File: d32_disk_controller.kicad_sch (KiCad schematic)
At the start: 25 parts, among them J1 Clock_Test, J2 IDC_Floppy, J3 EDGE, U1 27C64, U2 WD2797, U3 74HCT174, U4 74HCT139, U5 74HCT00, U6 74HCT04, U7 74LS07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

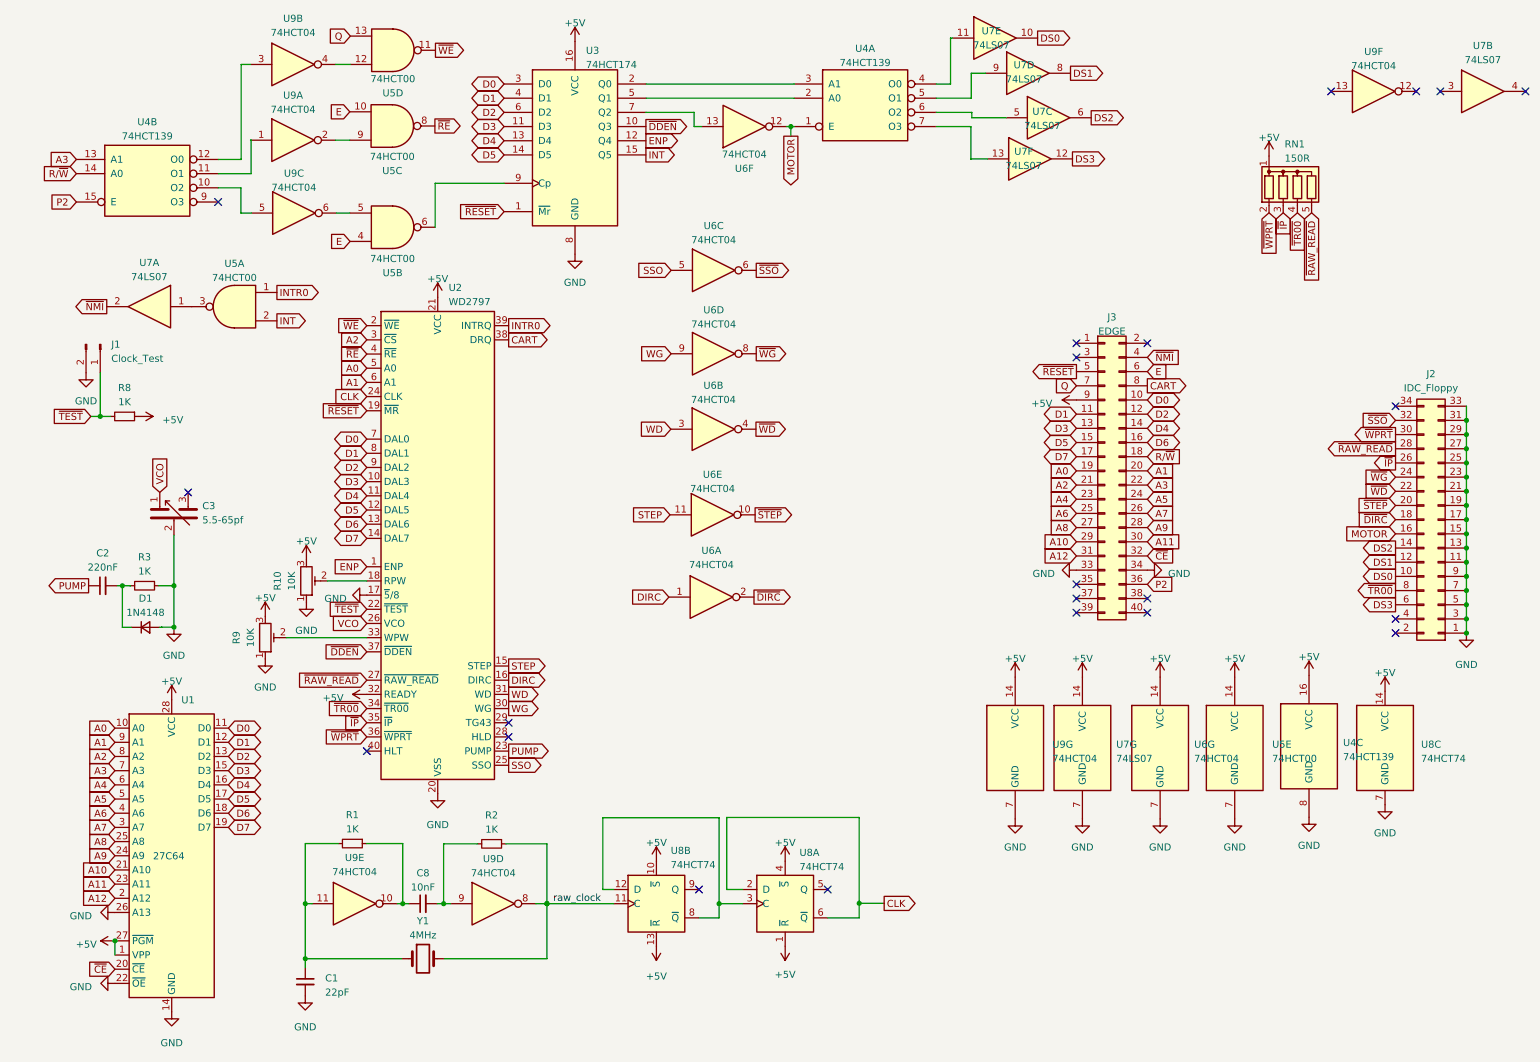
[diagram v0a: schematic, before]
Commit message: update from component selection change
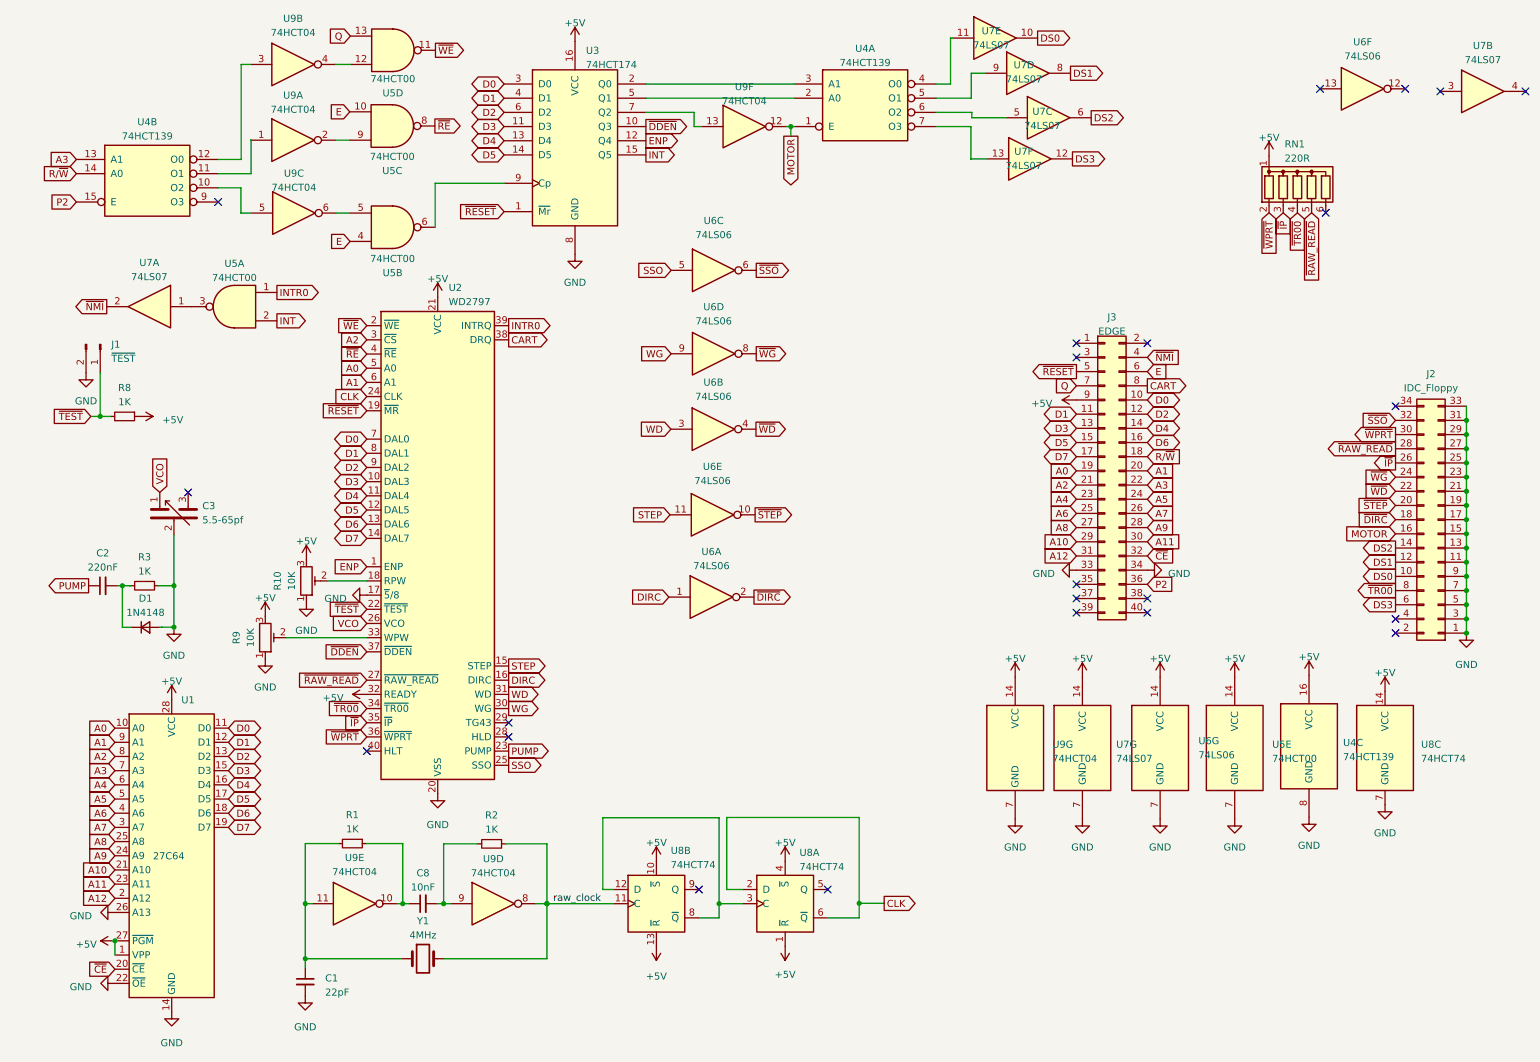
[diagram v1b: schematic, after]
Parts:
- removed U6: 74HCT04, Package_SO:SOIC-14_3.9x8.7mm_P1.27mm, symbol Dos_Controller:7416
- added U6: 74LS06, Package_SO:SOIC-14_3.9x8.7mm_P1.27mm, symbol 74xx:74LS06
- J1: value Clock_Test -> ~{TEST}
- J3: now left out of the parts list
- RN1: value 150R -> 220R; footprint Resistor_THT:R_Array_SIP5 -> Resistor_THT:R_Array_SIP6; symbol Device:R_Network04 -> Device:R_Network05
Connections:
- net +5V: now also U6.14 (VCC)
- net DIRC: now also U6.1
- net GND: now also U6.7 (GND)
- net MOTOR: now also U9.12
- net SSO: now also U6.5
- net STEP: now also U6.11
- net WD: now also U6.3
- net WG: now also U6.9
- net ~{DIRC}: now also U6.2
- net ~{SSO}: now also U6.6
- net ~{STEP}: now also U6.10
- net ~{WD}: now also U6.4
- net ~{WG}: now also U6.8
- net at U3.7 (Q2): now also U9.13
- no-connect marks 22 -> 23

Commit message: add test points
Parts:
- added J4: ~{MR}, TestPoint:TestPoint_2Pads_Pitch2.54mm_Drill0.8mm, symbol Connector:Conn_01x02_Pin
- added TP1: TestPoint_WD, TestPoint:TestPoint_Loop_D2.50mm_Drill1.0mm, symbol Connector:TestPoint_Probe
- added TP2: TestPoint_TG43, TestPoint:TestPoint_Loop_D2.50mm_Drill1.0mm, symbol Connector:TestPoint_Probe
- added TP3: TestPoint_Probe, TestPoint:TestPoint_Loop_D2.50mm_Drill1.0mm, symbol Connector:TestPoint_Probe
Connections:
- net DIRC: now also TP3.1
- net GND: now also J4.2 (Pin_2)
- net WD: now also TP1.1
- net ~{RESET}: now also J4.1 (Pin_1)
- net TG43: now reaches U2.29 (TG43)
- net TG43: now also TP2.1
- no-connect marks 23 -> 22
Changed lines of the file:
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@@
   (no_connect (at 198.4248 71.9836))
   (no_connect (at 198.4248 74.5236))
-  (no_connect (at 96.7232 139.954))
   (no_connect (at 71.3232 145.034))
   (no_connect (at 153.8732 169.8244))
@@
     )
   )
+  (global_label "~{RESET}" (shape input) (at 171.45 63.5 270) (fields_autoplaced)
+    (effects (font (size 1.27 1.27)) (justify right))
+    (property "Intersheetrefs" "${INTERSHEET_REFS}" (at 171.45 72.2303 90)
+      (effects (font (size 1.27 1.27)) (justify right) hide)
+    )
+  )
   (global_label "DS3" (shape output) (at 197.7136 38.9636 0) (fields_autoplaced)
     (effects (font (size 1.27 1.27)) (justify left))
@@
     )
   )
+  (global_label "TG43" (shape output) (at 161.036 87.122 180) (fields_autoplaced)
+    (effects (font (size 1.27 1.27)) (justify right))
+    (property "Intersheetrefs" "${INTERSHEET_REFS}" (at 153.3942 87.122 0)
+      (effects (font (size 1.27 1.27)) (justify right) hide)
+    )
+  )
   (global_label "A3" (shape input) (at 26.2128 148.5392 180) (fields_autoplaced)
     (effects (font (size 1.27 1.27)) (justify right))
@@
     )
   )
+  (global_label "TG43" (shape output) (at 96.7232 139.954 0) (fields_autoplaced)
+    (effects (font (size 1.27 1.27)) (justify left))
+    (property "Intersheetrefs" "${INTERSHEET_REFS}" (at 104.365 139.954 0)
+      (effects (font (size 1.27 1.27)) (justify left) hide)
+    )
+  )
   (global_label "A6" (shape input) (at 26.2128 156.1592 180) (fields_autoplaced)
     (effects (font (size 1.27 1.27)) (justify right))
@@
     )
   )
+  (global_label "DIRC" (shape output) (at 161.036 94.996 180) (fields_autoplaced)
+    (effects (font (size 1.27 1.27)) (justify right))
+    (property "Intersheetrefs" "${INTERSHEET_REFS}" (at 153.636 94.996 0)
+      (effects (font (size 1.27 1.27)) (justify right) hide)
+    )
+  )
   (global_label "E" (shape input) (at 211.1248 77.0636 0) (fields_autoplaced)
     (effects (font (size 1.27 1.27)) (justify left))
@@
     )
   )
+  (global_label "WD" (shape output) (at 160.782 78.994 180) (fields_autoplaced)
+    (effects (font (size 1.27 1.27)) (justify right))
+    (property "Intersheetrefs" "${INTERSHEET_REFS}" (at 155.0754 78.994 0)
+      (effects (font (size 1.27 1.27)) (justify right) hide)
+    )
+  )
   (global_label "~{IP}" (shape input) (at 71.3232 139.954 180) (fields_autoplaced)
     (effects (font (size 1.27 1.27)) (justify right))
@@
     )
   )
+  (symbol (lib_id "Connector:Conn_01x02_Pin") (at 171.45 58.42 270) (unit 1)
+    (in_bom yes) (on_board yes) (dnp no) (fields_autoplaced)
+    (property "Reference" "J4" (at 173.4312 58.42 90)
+      (effects (font (size 1.27 1.27)) (justify left))
+    )
+    (property "Value" "~{MR}" (at 173.4312 60.96 90)
+      (effects (font (size 1.27 1.27)) (justify left))
+    )
+    (property "Footprint" "TestPoint:TestPoint_2Pads_Pitch2.54mm_Drill0.8mm" (at 171.45 58.42 0)
+      (effects (font (size 1.27 1.27)) hide)
+    )
+    (property "Datasheet" "~" (at 171.45 58.42 0)
+      (effects (font (size 1.27 1.27)) hide)
+    )
+    (pin "1")
+    (pin "2")
+    (instances
+      (project "d32_disk_controller"
+        (path "/c5d711f3-7de6-4443-86e9-2b55dc097bf5"
+          (reference "J4") (unit 1)
+        )
+      )
+    )
+  )
   (symbol (lib_id "power:GND") (at 60.2996 188.8744 0) (unit 1)
     (in_bom yes) (on_board yes) (dnp no) (fields_autoplaced)
@@
     )
   )
+  (symbol (lib_id "power:GND") (at 168.91 63.5 0) (unit 1)
+    (in_bom yes) (on_board yes) (dnp no) (fields_autoplaced)
+    (property "Reference" "#PWR041" (at 168.91 69.85 0)
+      (effects (font (size 1.27 1.27)) hide)
+    )
+    (property "Value" "GND" (at 168.91 68.58 0)
+      (effects (font (size 1.27 1.27)))
+    )
+    (property "Footprint" "" (at 168.91 63.5 0)
+      (effects (font (size 1.27 1.27)) hide)
+    )
+    (property "Datasheet" "" (at 168.91 63.5 0)
+      (effects (font (size 1.27 1.27)) hide)
+    )
+    (pin "1")
+    (instances
+      (project "d32_disk_controller"
+        (path "/c5d711f3-7de6-4443-86e9-2b55dc097bf5"
+          (reference "#PWR041") (unit 1)
+        )
+      )
+    )
+  )
   (symbol (lib_id "Device:C_Small") (at 60.2996 186.3344 0) (unit 1)
     (in_bom yes) (on_board yes) (dnp no) (fields_autoplaced)
@@
     )
   )
+  (symbol (lib_id "Connector:TestPoint_Probe") (at 161.036 94.996 0) (unit 1)
+    (in_bom yes) (on_board yes) (dnp no)
+    (property "Reference" "TP3" (at 162.687 89.154 0)
+      (effects (font (size 1.27 1.27)))
+    )
+    (property "Value" "TestPoint_Probe" (at 162.687 90.932 0)
+      (effects (font (size 1.27 1.27)))
+    )
+    (property "Footprint" "TestPoint:TestPoint_Loop_D2.50mm_Drill1.0mm" (at 166.116 94.996 0)
+      (effects (font (size 1.27 1.27)) hide)
+    )
+    (property "Datasheet" "~" (at 166.116 94.996 0)
+      (effects (font (size 1.27 1.27)) hide)
+    )
+    (pin "1")
+    (instances
+      (project "d32_disk_controller"
+        (path "/c5d711f3-7de6-4443-86e9-2b55dc097bf5"
+          (reference "TP3") (unit 1)
+        )
+      )
+    )
+  )
   (symbol (lib_id "power:+5V") (at 123.19 179.9844 180) (unit 1)
     (in_bom yes) (on_board yes) (dnp no) (fields_autoplaced)
@@
     )
   )
+  (symbol (lib_id "Connector:TestPoint_Probe") (at 161.036 87.122 0) (unit 1)
+    (in_bom yes) (on_board yes) (dnp no)
+    (property "Reference" "TP2" (at 162.687 81.28 0)
+      (effects (font (size 1.27 1.27)))
+    )
+    (property "Value" "TestPoint_TG43" (at 162.687 83.058 0)
+      (effects (font (size 1.27 1.27)))
+    )
+    (property "Footprint" "TestPoint:TestPoint_Loop_D2.50mm_Drill1.0mm" (at 166.116 87.122 0)
+      (effects (font (size 1.27 1.27)) hide)
+    )
+    (property "Datasheet" "~" (at 166.116 87.122 0)
+      (effects (font (size 1.27 1.27)) hide)
+    )
+    (pin "1")
+    (instances
+      (project "d32_disk_controller"
+        (path "/c5d711f3-7de6-4443-86e9-2b55dc097bf5"
+          (reference "TP2") (unit 1)
+        )
+      )
+    )
+  )
   (symbol (lib_id "74xx:74LS04") (at 187.452 144.4752 0) (unit 7)
     (in_bom yes) (on_board yes) (dnp no) (fields_autoplaced)
@@
         )
       )
+    )
+  )
+  (symbol (lib_id "Connector:TestPoint_Probe") (at 160.782 78.994 0) (unit 1)
+    (in_bom yes) (on_board yes) (dnp no) (fields_autoplaced)
+    (property "Reference" "TP1" (at 165.1 76.1365 0)
+      (effects (font (size 1.27 1.27)) (justify left))
+    )
+    (property "Value" "TestPoint_WD" (at 165.1 78.6765 0)
+      (effects (font (size 1.27 1.27)) (justify left))
+    )
+    (property "Footprint" "TestPoint:TestPoint_Loop_D2.50mm_Drill1.0mm" (at 165.862 78.994 0)
+      (effects (font (size 1.27 1.27)) hide)
+    )
+    (property "Datasheet" "~" (at 165.862 78.994 0)
+      (effects (font (size 1.27 1.27)) hide)
+    )
+    (pin "1")
+    (instances
+      (project "d32_disk_controller"
+        (path "/c5d711f3-7de6-4443-86e9-2b55dc097bf5"
+          (reference "TP1") (unit 1)
+        )
+      )
